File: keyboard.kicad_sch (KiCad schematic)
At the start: 30 parts, among them IC2 80C51, IC3 74LS145, IC4 74LS145, IC7 74LS366, IC9 74LS241

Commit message: fix footprint sizes
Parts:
- RX2: footprint Resistor_THT:R_Axial_DIN0204_L3.6mm_D1.6mm_P5.08mm_Horizontal -> Resistor_THT:R_Axial_DIN0204_L3.6mm_D1.6mm_P7.62mm_Horizontal
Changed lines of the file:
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@@
 			)
 		)
-		(property "Footprint" "Resistor_THT:R_Axial_DIN0204_L3.6mm_D1.6mm_P5.08mm_Horizontal"
+		(property "Footprint" "Resistor_THT:R_Axial_DIN0204_L3.6mm_D1.6mm_P7.62mm_Horizontal"
 			(at 151.13 237.49 0)
 			(effects

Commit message: enlarge J-leg footprints
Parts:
- IC2: footprint Package_LCC:PLCC-44_16.6x16.6mm_P1.27mm -> Acorn:PLCC-44
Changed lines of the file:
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@@
 			)
 		)
-		(property "Footprint" "Package_LCC:PLCC-44_16.6x16.6mm_P1.27mm"
+		(property "Footprint" "Acorn:PLCC-44"
 			(at 77.47 165.1 0)
 			(effects

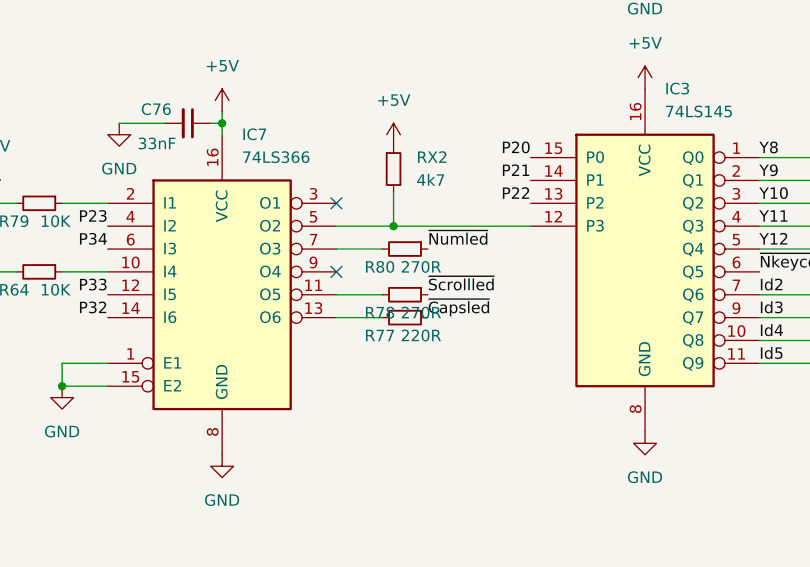
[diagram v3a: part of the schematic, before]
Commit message: adjust shielding perimeter trace and mounting holes
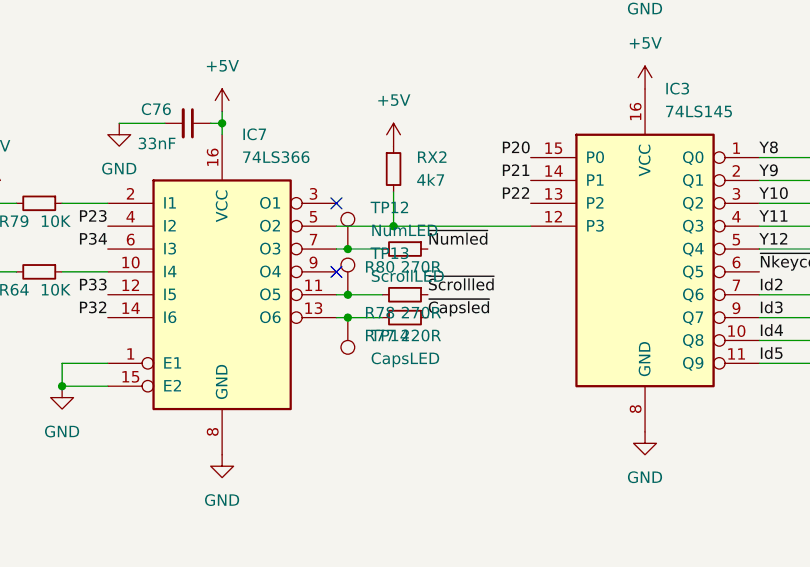
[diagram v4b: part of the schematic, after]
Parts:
- added TP12: NumLED, TestPoint:TestPoint_Pad_D1.0mm, symbol Connector:TestPoint
- added TP13: ScrollLED, TestPoint:TestPoint_Pad_D1.0mm, symbol Connector:TestPoint
- added TP14: CapsLED, TestPoint:TestPoint_Pad_D1.0mm, symbol Connector:TestPoint
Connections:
- net at IC7.11 (O5), R78.2: now also TP13.1
- net at IC7.13 (O6), R77.2: now also TP14.1
- net at IC7.7 (O3), R80.2: now also TP12.1

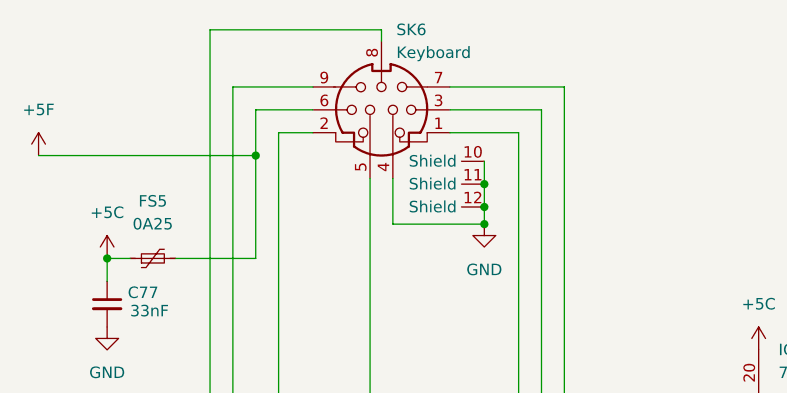
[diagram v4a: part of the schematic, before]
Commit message: add ide and rework onboard ram
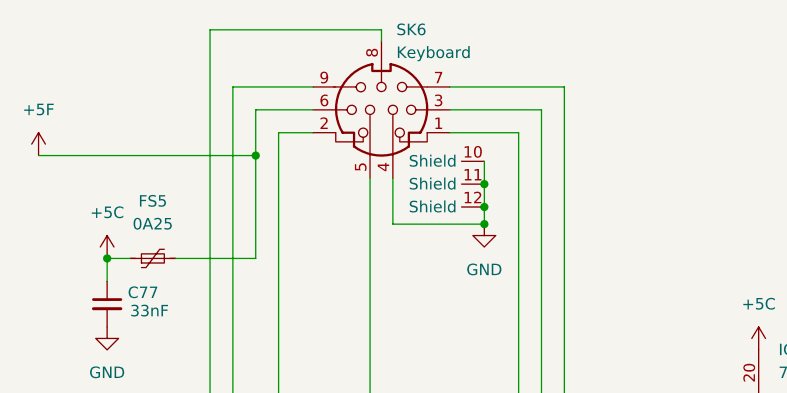
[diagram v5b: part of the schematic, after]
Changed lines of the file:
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@@
 (kicad_sch
-	(version 20231120)
+	(version 20250114)
 	(generator "eeschema")
-	(generator_version "8.0")
+	(generator_version "9.0")
 	(paper "A3")
 	(title_block
@@
 		)
 		(instances
-			(project ""
+			(project "Acorn-A3010"
 				(path "/999882f3-94f8-4a89-9093-27a47d0cb289/20613dd3-c886-4190-96bd-e62e2e571bea"
 					(reference "SK6")
@@
 		)
 		(instances
-			(project ""
+			(project "Acorn-A3010"
 				(path "/999882f3-94f8-4a89-9093-27a47d0cb289/20613dd3-c886-4190-96bd-e62e2e571bea"
 					(reference "RP3")
@@
 		)
 		(instances
-			(project ""
+			(project "Acorn-A3010"
 				(path "/999882f3-94f8-4a89-9093-27a47d0cb289/20613dd3-c886-4190-96bd-e62e2e571bea"
 					(reference "RP3")
@@
 		)
 		(instances
-			(project ""
+			(project "Acorn-A3010"
 				(path "/999882f3-94f8-4a89-9093-27a47d0cb289/20613dd3-c886-4190-96bd-e62e2e571bea"
 					(reference "RP3")
@@
 		)
 		(instances
-			(project ""
+			(project "Acorn-A3010"
 				(path "/999882f3-94f8-4a89-9093-27a47d0cb289/20613dd3-c886-4190-96bd-e62e2e571bea"
 					(reference "RP3")
@@
 		)
 		(instances
-			(project ""
+			(project "Acorn-A3010"
 				(path "/999882f3-94f8-4a89-9093-27a47d0cb289/20613dd3-c886-4190-96bd-e62e2e571bea"
 					(reference "RP3")
@@
 		)
 		(instances
-			(project ""
+			(project "Acorn-A3010"
 				(path "/999882f3-94f8-4a89-9093-27a47d0cb289/20613dd3-c886-4190-96bd-e62e2e571bea"
 					(reference "RP3")
@@
 		)
 		(instances
-			(project ""
+			(project "Acorn-A3010"
 				(path "/999882f3-94f8-4a89-9093-27a47d0cb289/20613dd3-c886-4190-96bd-e62e2e571bea"
 					(reference "IC7")
@@
 		)
 		(instances
-			(project ""
+			(project "Acorn-A3010"
 				(path "/999882f3-94f8-4a89-9093-27a47d0cb289/20613dd3-c886-4190-96bd-e62e2e571bea"
 					(reference "RP3")
@@
 		)
 		(instances
-			(project ""
+			(project "Acorn-A3010"
 				(path "/999882f3-94f8-4a89-9093-27a47d0cb289/20613dd3-c886-4190-96bd-e62e2e571bea"
 					(reference "#PWR0156")
@@
 		)
 		(instances
-			(project ""
+			(project "Acorn-A3010"
 				(path "/999882f3-94f8-4a89-9093-27a47d0cb289/20613dd3-c886-4190-96bd-e62e2e571bea"
 					(reference "IC4")
@@
 		)
 		(instances
-			(project ""
+			(project "Acorn-A3010"
 				(path "/999882f3-94f8-4a89-9093-27a47d0cb289/20613dd3-c886-4190-96bd-e62e2e571bea"
 					(reference "RP3")
@@
 		)
 		(instances
-			(project ""
+			(project "Acorn-A3010"
 				(path "/999882f3-94f8-4a89-9093-27a47d0cb289/20613dd3-c886-4190-96bd-e62e2e571bea"
 					(reference "RP3")
@@
 		)
 		(instances
-			(project ""
+			(project "Acorn-A3010"
 				(path "/999882f3-94f8-4a89-9093-27a47d0cb289/20613dd3-c886-4190-96bd-e62e2e571bea"
 					(reference "RP3")
@@
 		)
 		(instances
-			(project ""
+			(project "Acorn-A3010"
 				(path "/999882f3-94f8-4a89-9093-27a47d0cb289/20613dd3-c886-4190-96bd-e62e2e571bea"
 					(reference "FS5")
@@
 		)
 		(instances
-			(project ""
+			(project "Acorn-A3010"
 				(path "/999882f3-94f8-4a89-9093-27a47d0cb289/20613dd3-c886-4190-96bd-e62e2e571bea"
 					(reference "RP3")
@@
 		)
 		(instances
-			(project ""
+			(project "Acorn-A3010"
 				(path "/999882f3-94f8-4a89-9093-27a47d0cb289/20613dd3-c886-4190-96bd-e62e2e571bea"
 					(reference "RP3")
@@
 		)
 		(instances
-			(project ""
+			(project "Acorn-A3010"
 				(path "/999882f3-94f8-4a89-9093-27a47d0cb289/20613dd3-c886-4190-96bd-e62e2e571bea"
 					(reference "RP3")
@@
 		)
 		(instances
-			(project ""
+			(project "Acorn-A3010"
 				(path "/999882f3-94f8-4a89-9093-27a47d0cb289/20613dd3-c886-4190-96bd-e62e2e571bea"
 					(reference "SK2")
@@
 		)
 		(instances
-			(project ""
+			(project "Acorn-A3010"
 				(path "/999882f3-94f8-4a89-9093-27a47d0cb289/20613dd3-c886-4190-96bd-e62e2e571bea"
 					(reference "LK7")
@@
 		)
 		(instances
-			(project ""
+			(project "Acorn-A3010"
 				(path "/999882f3-94f8-4a89-9093-27a47d0cb289/20613dd3-c886-4190-96bd-e62e2e571bea"
 					(reference "IC9")
@@
 		)
 		(instances
-			(project ""
+			(project "Acorn-A3010"
 				(path "/999882f3-94f8-4a89-9093-27a47d0cb289/20613dd3-c886-4190-96bd-e62e2e571bea"
 					(reference "RP3")
@@
 		)
 		(instances
-			(project ""
+			(project "Acorn-A3010"
 				(path "/999882f3-94f8-4a89-9093-27a47d0cb289/20613dd3-c886-4190-96bd-e62e2e571bea"
 					(reference "#PWR0163")
@@
 		)
 		(instances
-			(project ""
+			(project "Acorn-A3010"
 				(path "/999882f3-94f8-4a89-9093-27a47d0cb289/20613dd3-c886-4190-96bd-e62e2e571bea"
 					(reference "#PWR0159")
@@
 		)
 		(instances
-			(project ""
+			(project "Acorn-A3010"
 				(path "/999882f3-94f8-4a89-9093-27a47d0cb289/20613dd3-c886-4190-96bd-e62e2e571bea"
 					(reference "RX2")
@@
 		)
 		(instances
-			(project ""
+			(project "Acorn-A3010"
 				(path "/999882f3-94f8-4a89-9093-27a47d0cb289/20613dd3-c886-4190-96bd-e62e2e571bea"
 					(reference "RP3")
@@
 		)
 		(instances
-			(project ""
+			(project "Acorn-A3010"
 				(path "/999882f3-94f8-4a89-9093-27a47d0cb289/20613dd3-c886-4190-96bd-e62e2e571bea"
 					(reference "IC2")
